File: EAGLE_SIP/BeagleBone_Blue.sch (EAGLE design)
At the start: 265 parts, among them M1 JST_ZH_2, M2 JST_ZH_2, M3 JST_ZH_2, M4 JST_ZH_2, P10 SCHA5B0200, Q3 MOSFET-N, U1 TPD4S012_DRY_6, U4 TPD4S012_DRY_6, U5 24LC_32AT-I/OT, U6 SN74LVC1G07_DCK_5, U7 TPS2051B_D_8, U8 MTFC4GLDEA, Y1 CM200C-32.768KAZF-UT, Y2 445C33D24M00000

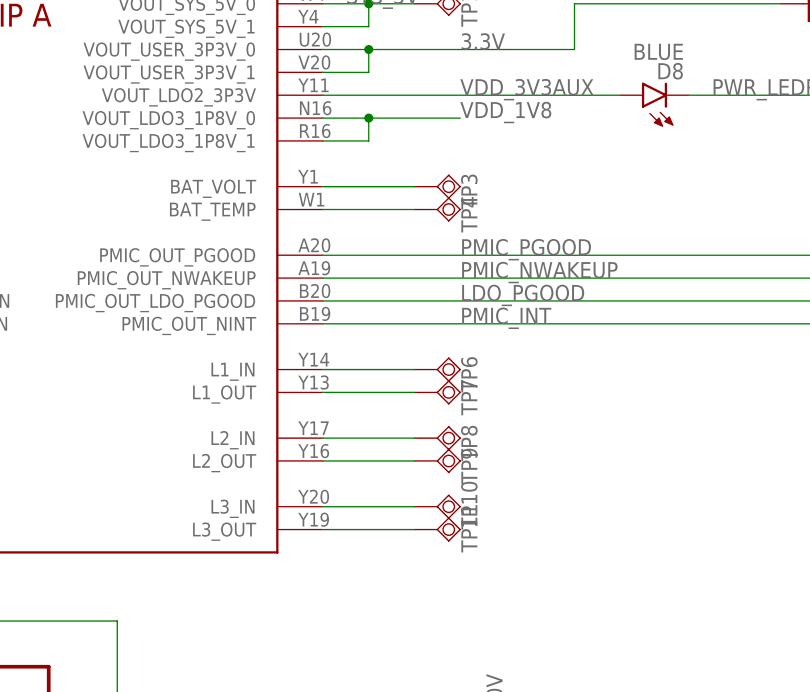
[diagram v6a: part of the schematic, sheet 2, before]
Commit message: Delete some test points I know I will not use
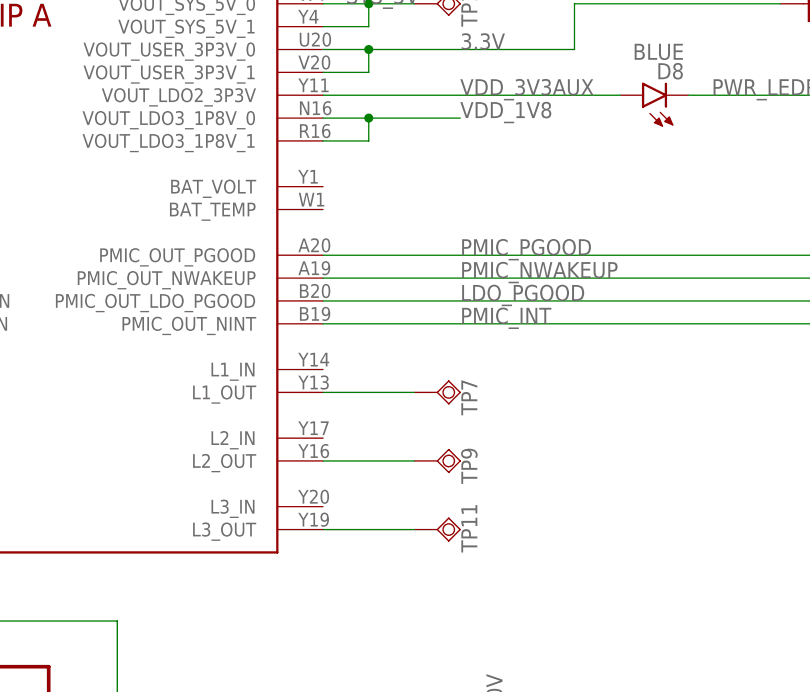
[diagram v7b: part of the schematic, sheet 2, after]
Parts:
- removed TP10, TP3, TP4, TP6, TP8: TPSQB1,27, testpad:TPSQB1,27
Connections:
- removed net N$13: SIPA.L1_IN, TP6.TP
- removed net N$20: SIPA.L2_IN, TP8.TP
- removed net N$22: SIPA.L3_IN, TP10.TP
- removed net N$7: SIPA.BAT_VOLT, TP3.TP
- removed net N$9: SIPA.BAT_TEMP, TP4.TP
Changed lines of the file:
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@@
 <part name="TP1" library="testpad" deviceset="TPSQ" device="B1,27"/>
 <part name="TP2" library="testpad" deviceset="TPSQ" device="B1,27"/>
-<part name="TP3" library="testpad" deviceset="TPSQ" device="B1,27"/>
-<part name="TP4" library="testpad" deviceset="TPSQ" device="B1,27"/>
 <part name="TP5" library="testpad" deviceset="TPSQ" device="B1,27"/>
 <part name="R2" library="Strawson_Eagle_Lib" deviceset="RESISTOR" device="0402-RES" value="1.5K,1%"/>
@@
 <part name="D8" library="BeagleBone_Blue" deviceset="LED" device="0603" value="BLUE"/>
 <part name="R24" library="Strawson_Eagle_Lib" deviceset="RESISTOR" device="0402-RES" value="4.75K,1%"/>
-<part name="TP6" library="testpad" deviceset="TPSQ" device="B1,27"/>
 <part name="TP7" library="testpad" deviceset="TPSQ" device="B1,27"/>
-<part name="TP8" library="testpad" deviceset="TPSQ" device="B1,27"/>
 <part name="TP9" library="testpad" deviceset="TPSQ" device="B1,27"/>
-<part name="TP10" library="testpad" deviceset="TPSQ" device="B1,27"/>
 <part name="TP11" library="testpad" deviceset="TPSQ" device="B1,27"/>
 <part name="TP12" library="testpad" deviceset="TPSQ" device="B1,27"/>
@@
 <instance part="TP1" gate="G$1" x="137.16" y="243.84" rot="R90"/>
 <instance part="TP2" gate="G$1" x="45.72" y="223.52" rot="R270"/>
-<instance part="TP3" gate="G$1" x="137.16" y="223.52" rot="R90"/>
-<instance part="TP4" gate="G$1" x="137.16" y="220.98" rot="R90"/>
 <instance part="TP5" gate="G$1" x="45.72" y="210.82" rot="R270"/>
 <instance part="R2" gate="G$1" x="38.1" y="198.12" rot="R90"/>
@@
 <instance part="D8" gate="G$1" x="160.02" y="233.68" rot="R90"/>
 <instance part="R24" gate="G$1" x="193.04" y="233.68"/>
-<instance part="TP6" gate="G$1" x="137.16" y="203.2" rot="R90"/>
 <instance part="TP7" gate="G$1" x="137.16" y="200.66" rot="R90"/>
-<instance part="TP8" gate="G$1" x="137.16" y="195.58" rot="R90"/>
 <instance part="TP9" gate="G$1" x="137.16" y="193.04" rot="R90"/>
-<instance part="TP10" gate="G$1" x="137.16" y="187.96" rot="R90"/>
 <instance part="TP11" gate="G$1" x="137.16" y="185.42" rot="R90"/>
 <instance part="TP12" gate="G$1" x="208.28" y="243.84" rot="R90"/>
@@
 </segment>
 </net>
-<net name="N$7" class="0">
-<segment>
-<pinref part="SIP" gate="A" pin="BAT_VOLT"/>
-<pinref part="TP3" gate="G$1" pin="TP"/>
-<wire x1="124.46" y1="223.52" x2="134.62" y2="223.52" width="0.1524" layer="91"/>
-</segment>
-</net>
-<net name="N$9" class="0">
-<segment>
-<pinref part="SIP" gate="A" pin="BAT_TEMP"/>
-<pinref part="TP4" gate="G$1" pin="TP"/>
-<wire x1="124.46" y1="220.98" x2="134.62" y2="220.98" width="0.1524" layer="91"/>
-</segment>
-</net>
 <net name="N$12" class="0">
 <segment>
@@
 </segment>
 </net>
-<net name="N$13" class="0">
-<segment>
-<pinref part="SIP" gate="A" pin="L1_IN"/>
-<pinref part="TP6" gate="G$1" pin="TP"/>
-<wire x1="124.46" y1="203.2" x2="134.62" y2="203.2" width="0.1524" layer="91"/>
-</segment>
-</net>
 <net name="N$19" class="0">
 <segment>
@@
 </segment>
 </net>
-<net name="N$20" class="0">
-<segment>
-<pinref part="SIP" gate="A" pin="L2_IN"/>
-<pinref part="TP8" gate="G$1" pin="TP"/>
-<wire x1="124.46" y1="195.58" x2="134.62" y2="195.58" width="0.1524" layer="91"/>
-</segment>
-</net>
 <net name="N$21" class="0">
 <segment>
@@
 </segment>
 </net>
-<net name="N$22" class="0">
-<segment>
-<pinref part="SIP" gate="A" pin="L3_IN"/>
-<pinref part="TP10" gate="G$1" pin="TP"/>
-<wire x1="124.46" y1="187.96" x2="134.62" y2="187.96" width="0.1524" layer="91"/>
-</segment>
-</net>

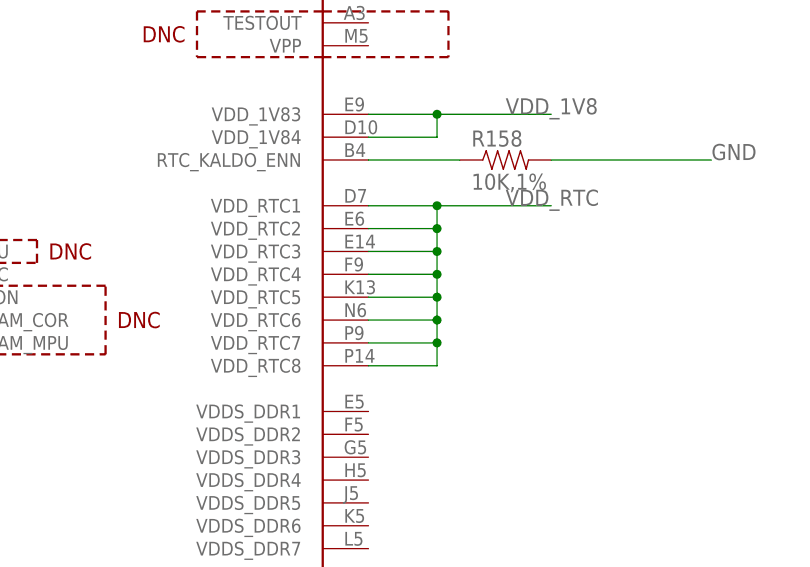
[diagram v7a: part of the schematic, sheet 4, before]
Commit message: Delete extraneous VDD_RTC connections and save shortest route
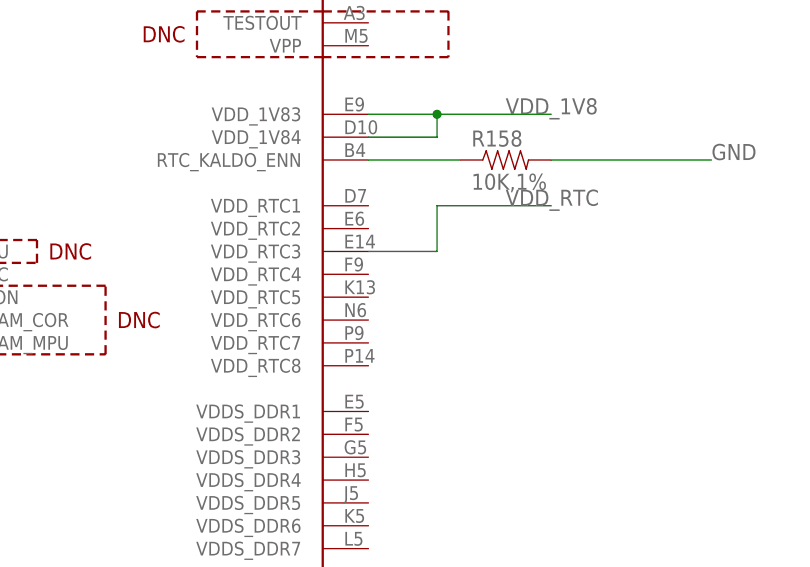
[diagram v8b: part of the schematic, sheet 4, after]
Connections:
- net VDD_RTC: no longer SIPE.VDD_RTC1, SIPE.VDD_RTC2, SIPE.VDD_RTC4, SIPE.VDD_RTC5, SIPE.VDD_RTC6, SIPE.VDD_RTC7, SIPE.VDD_RTC8
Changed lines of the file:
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@@
 <net name="VDD_RTC" class="0">
 <segment>
-<pinref part="SIP" gate="E" pin="VDD_RTC1"/>
-<wire x1="134.62" y1="152.4" x2="142.24" y2="152.4" width="0.1524" layer="91"/>
 <wire x1="154.94" y1="152.4" x2="142.24" y2="152.4" width="0.1524" layer="91"/>
-<pinref part="SIP" gate="E" pin="VDD_RTC2"/>
-<wire x1="134.62" y1="149.86" x2="142.24" y2="149.86" width="0.1524" layer="91"/>
-<wire x1="142.24" y1="149.86" x2="142.24" y2="152.4" width="0.1524" layer="91"/>
-<junction x="142.24" y="152.4"/>
 <pinref part="SIP" gate="E" pin="VDD_RTC3"/>
 <wire x1="134.62" y1="147.32" x2="142.24" y2="147.32" width="0.1524" layer="91"/>
-<wire x1="142.24" y1="147.32" x2="142.24" y2="149.86" width="0.1524" layer="91"/>
-<junction x="142.24" y="149.86"/>
-<pinref part="SIP" gate="E" pin="VDD_RTC4"/>
-<wire x1="134.62" y1="144.78" x2="142.24" y2="144.78" width="0.1524" layer="91"/>
-<wire x1="142.24" y1="144.78" x2="142.24" y2="147.32" width="0.1524" layer="91"/>
-<junction x="142.24" y="147.32"/>
-<pinref part="SIP" gate="E" pin="VDD_RTC5"/>
-<wire x1="134.62" y1="142.24" x2="142.24" y2="142.24" width="0.1524" layer="91"/>
-<wire x1="142.24" y1="142.24" x2="142.24" y2="144.78" width="0.1524" layer="91"/>
-<junction x="142.24" y="144.78"/>
-<pinref part="SIP" gate="E" pin="VDD_RTC6"/>
-<wire x1="134.62" y1="139.7" x2="142.24" y2="139.7" width="0.1524" layer="91"/>
-<wire x1="142.24" y1="139.7" x2="142.24" y2="142.24" width="0.1524" layer="91"/>
-<junction x="142.24" y="142.24"/>
-<pinref part="SIP" gate="E" pin="VDD_RTC7"/>
-<wire x1="134.62" y1="137.16" x2="142.24" y2="137.16" width="0.1524" layer="91"/>
-<wire x1="142.24" y1="137.16" x2="142.24" y2="139.7" width="0.1524" layer="91"/>
-<junction x="142.24" y="139.7"/>
-<pinref part="SIP" gate="E" pin="VDD_RTC8"/>
-<wire x1="134.62" y1="134.62" x2="142.24" y2="134.62" width="0.1524" layer="91"/>
-<wire x1="142.24" y1="134.62" x2="142.24" y2="137.16" width="0.1524" layer="91"/>
-<junction x="142.24" y="137.16"/>
+<wire x1="142.24" y1="147.32" x2="142.24" y2="152.4" width="0.1524" layer="91"/>
 <label x="149.86" y="152.4" size="1.778" layer="95"/>
 </segment>
